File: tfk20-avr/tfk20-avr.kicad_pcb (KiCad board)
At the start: 4 copper layers, 76.2 x 115.9 mm, 122 parts, among them J1 USB_C_Receptacle_USB2.0, J2 AVR-ISP-6, SW1 Reset, U1 ATmega32U4-AU, U2 IS31FL3733-TQ, Y1 16MHz

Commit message: Finish routing
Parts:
- moved R13 8.08 mm to (181.9, 89.3), turned to 90 degrees
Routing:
- net GND: track 103.1 -> 236.1 mm, vias 16 -> 37
- net (no net): track 0.00 -> 21.8 mm
- net /tfk20 RGB Matrix/SW4: track 135.7 -> 146.7 mm, vias 16 -> 17
- net Net-(R13-Pad2): track 2.82 -> 7.60 mm
- net Net-(C8-Pad1): track 1.27 -> 5.77 mm
- net /tfk20 RGB Matrix/CS8: track 111.4 -> 115.2 mm, vias 10 -> 11
- net +5V: track 334.2 -> 336.9 mm
- net Net-(R7-Pad2): track 9.91 -> 12.3 mm
- net /COL_3: track 86.7 -> 88.1 mm
- net /tfk20 RGB Matrix/SW8: track 204.4 -> 203.2 mm
- net /tfk20 RGB Matrix/SW7: track 225.2 -> 224.4 mm
- net /RGB_MATRIX_SCL: track 31.7 -> 32.3 mm
- net /RGB_MATRIX_SDA: track 29.0 -> 29.6 mm
- net /XTAL2: vias 0 -> 2
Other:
- copper layers 4 -> 2

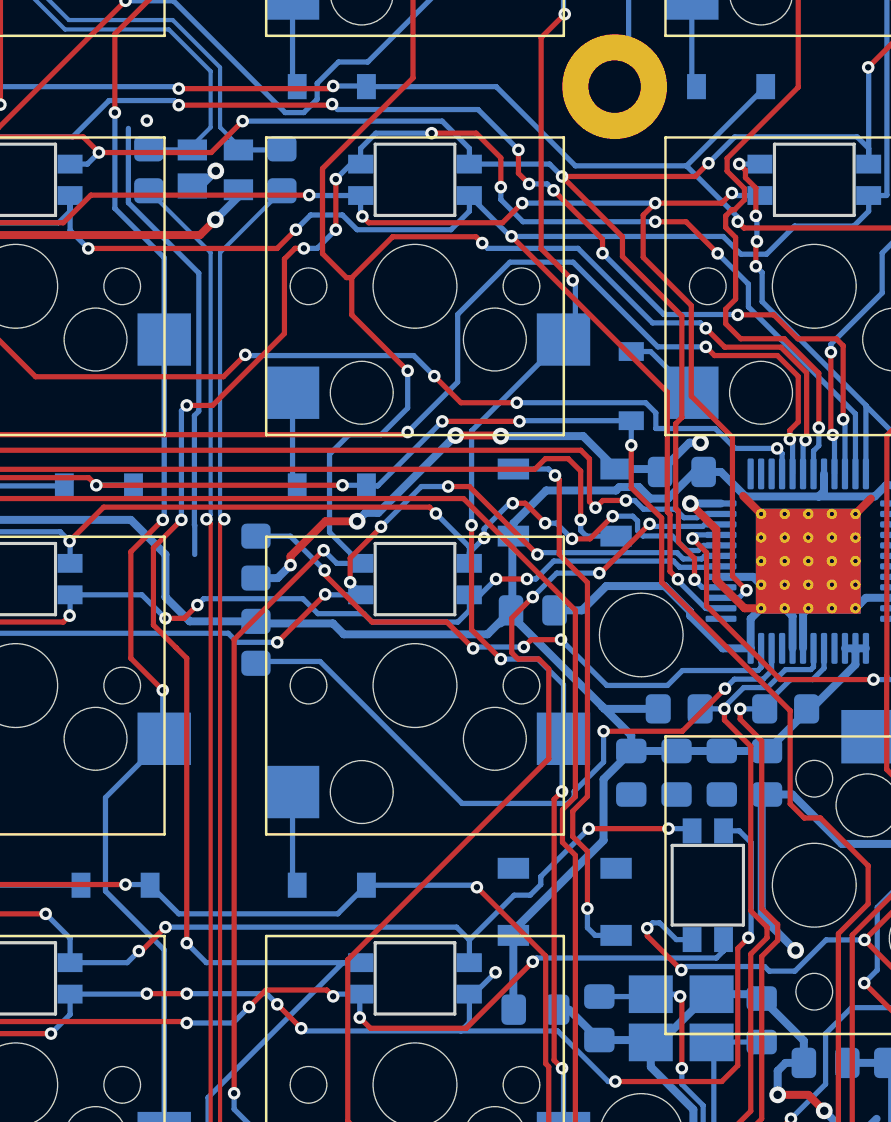
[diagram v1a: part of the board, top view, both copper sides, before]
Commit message: Add dimensions
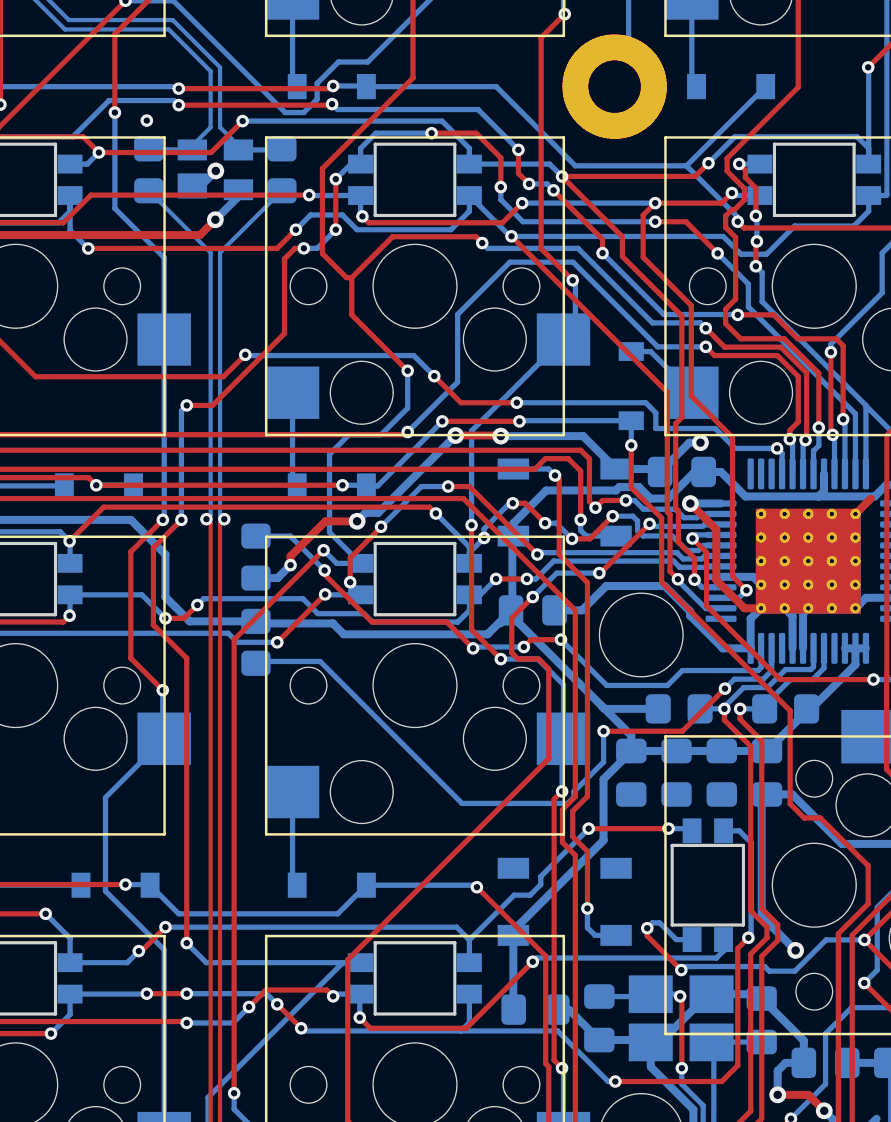
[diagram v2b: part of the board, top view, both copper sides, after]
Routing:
- net (no net): track 21.8 -> 0.00 mm
- net /tfk20 RGB Matrix/SW4: track 146.7 -> 145.2 mm, vias 17 -> 16
- net GND: track 236.1 -> 234.9 mm

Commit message: Tweak some things
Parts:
- moved SW1 1.19 mm to (126.2, 78.2)
- moved J1 0.56 mm to (125.8, 40.1)
- moved R1 0.13 mm to (125.3, 85.3)
- moved R2 0.13 mm to (120.7, 46.4)
- moved R3 0.13 mm to (131.7, 46.4)
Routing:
- net GND: track 234.9 -> 240.5 mm, vias 37 -> 38
- net /tfk20 RGB Matrix/SW9: track 246.7 -> 249.6 mm
- net /RESET: track 143.6 -> 144.3 mm
- net /tfk20 RGB Matrix/SW5: track 149.9 -> 150.5 mm
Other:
- board size 76.2 x 115.9 mm -> 76.2 x 115.5 mm
- board text added: "Inner hole diameter: 2.5mm"
- board text added: "tfk20 biosmanager Rev. 0"

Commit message: Add signature
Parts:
- added G1: LOGO, biosmanager:biosmanager_logo_filled_alt, F.Cu at (145.3, 77.0)
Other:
- board text added: "Rev. 0"
- board text added: "tfk20-avr Designed by biosmanager"
- board text removed: "tfk20 biosmanager Rev. 0"

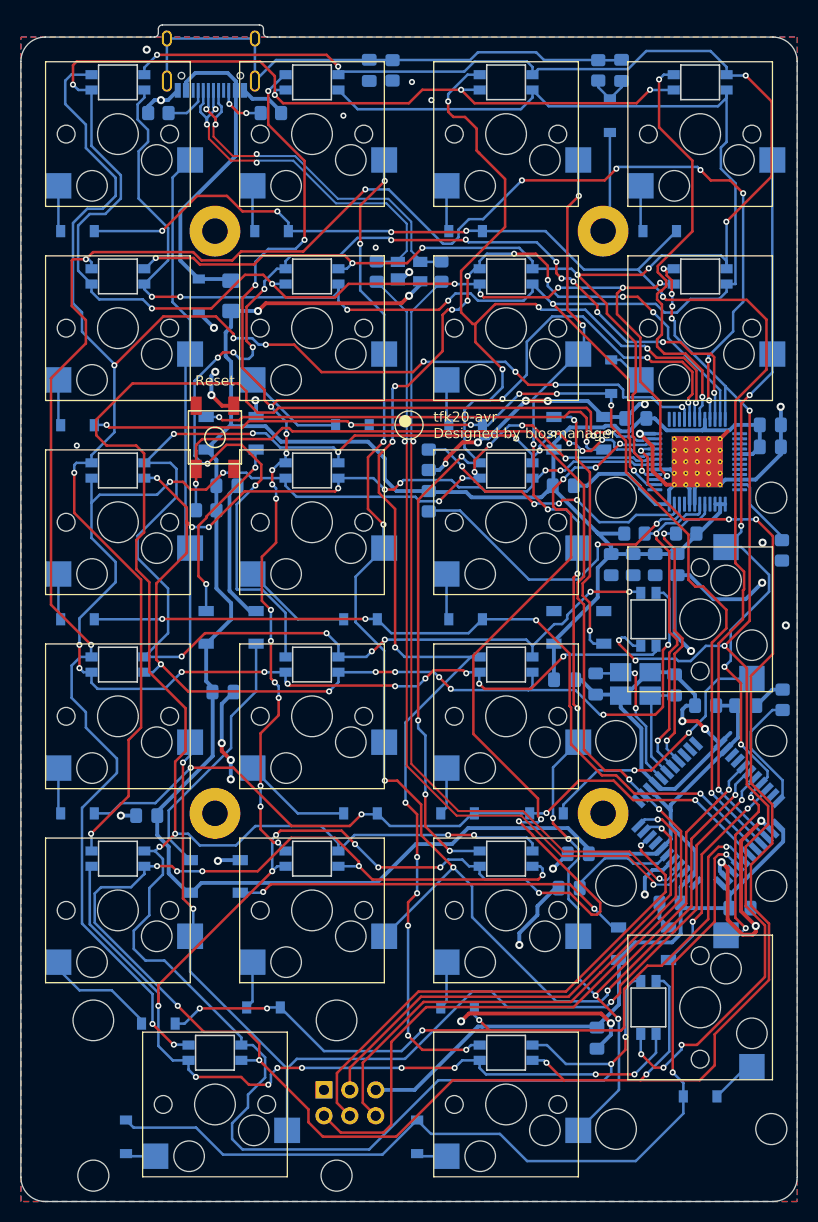
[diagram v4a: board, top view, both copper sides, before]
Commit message: Start new 4 layer layout
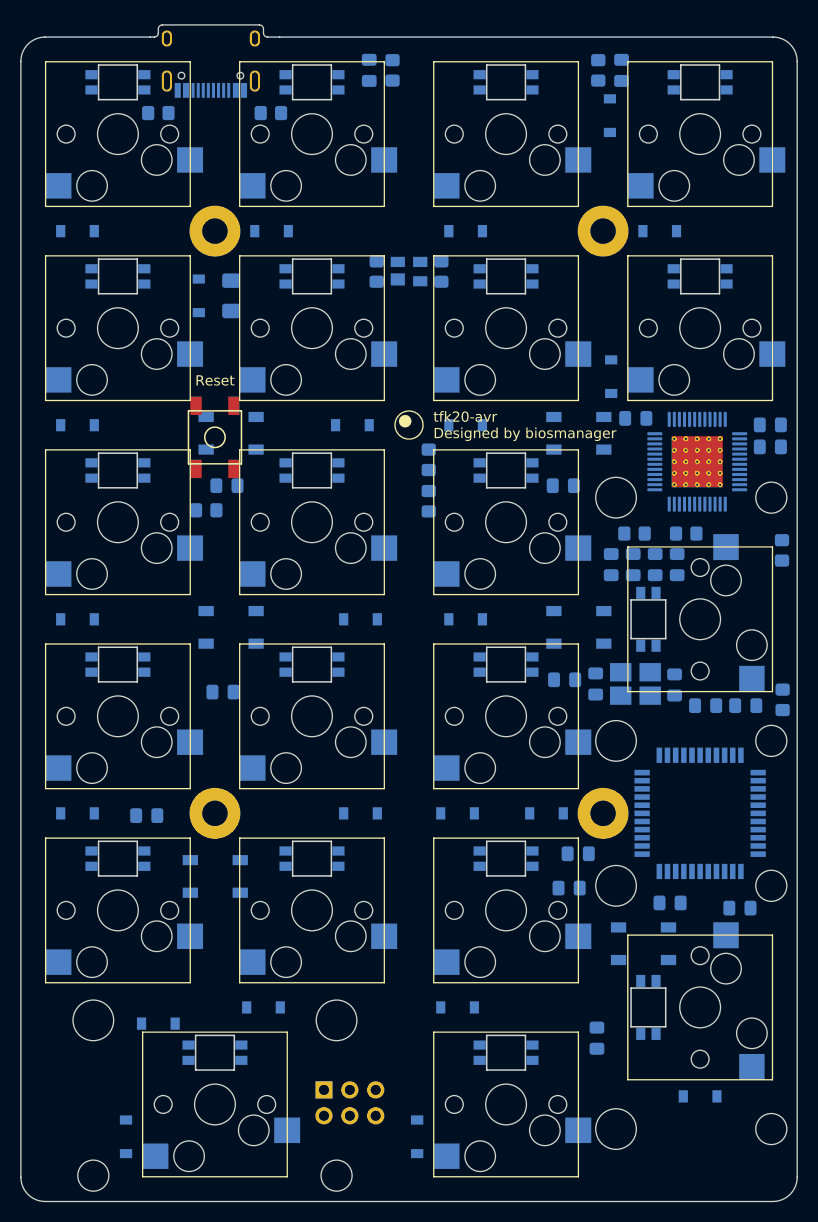
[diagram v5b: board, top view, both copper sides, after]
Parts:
- moved U1 0.79 mm to (173.8, 115.1), turned to 0 degrees
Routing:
- net +5V: track 336.9 -> 0.00 mm, vias 2 -> 0
- net /tfk20 RGB Matrix/SW9: track 249.6 -> 0.00 mm, vias 8 -> 0
- net GND: track 240.5 -> 0.00 mm, vias 38 -> 0
- net /tfk20 RGB Matrix/SW7: track 224.4 -> 0.00 mm, vias 12 -> 0
- net /tfk20 RGB Matrix/SW8: track 203.2 -> 0.00 mm, vias 20 -> 0
- net /tfk20 RGB Matrix/CS5: track 192.1 -> 0.00 mm, vias 11 -> 0
- net /tfk20 RGB Matrix/SW2: track 180.8 -> 0.00 mm, vias 12 -> 0
- net /tfk20 RGB Matrix/SW3: track 174.9 -> 0.00 mm, vias 10 -> 0
- net /tfk20 RGB Matrix/SW1: track 173.0 -> 0.00 mm, vias 6 -> 0
- net /COL_0: track 165.4 -> 0.00 mm, vias 4 -> 0
- net /tfk20 RGB Matrix/CS1: track 156.3 -> 0.00 mm, vias 9 -> 0
- net /tfk20 RGB Matrix/SW5: track 150.5 -> 0.00 mm, vias 18 -> 0
- net /tfk20 RGB Matrix/SW4: track 145.2 -> 0.00 mm, vias 16 -> 0
- net /RESET: track 144.3 -> 0.00 mm, vias 3 -> 0
- net /tfk20 RGB Matrix/CS2: track 142.7 -> 0.00 mm, vias 19 -> 0
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- added copper zone on POWER, net +5V
- added copper zone on GND, net GND
- removed copper zone on B.Cu, net GND
- removed copper zone on F.Cu, net GND
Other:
- copper layers 2 -> 4
- net class Default: clearance 0.15 -> 0.1524; trace_width 0.25 -> 0.254
- net class Power: clearance 0.15 -> 0.1524
- rule trace_clearance: 0.15 -> 0.1524

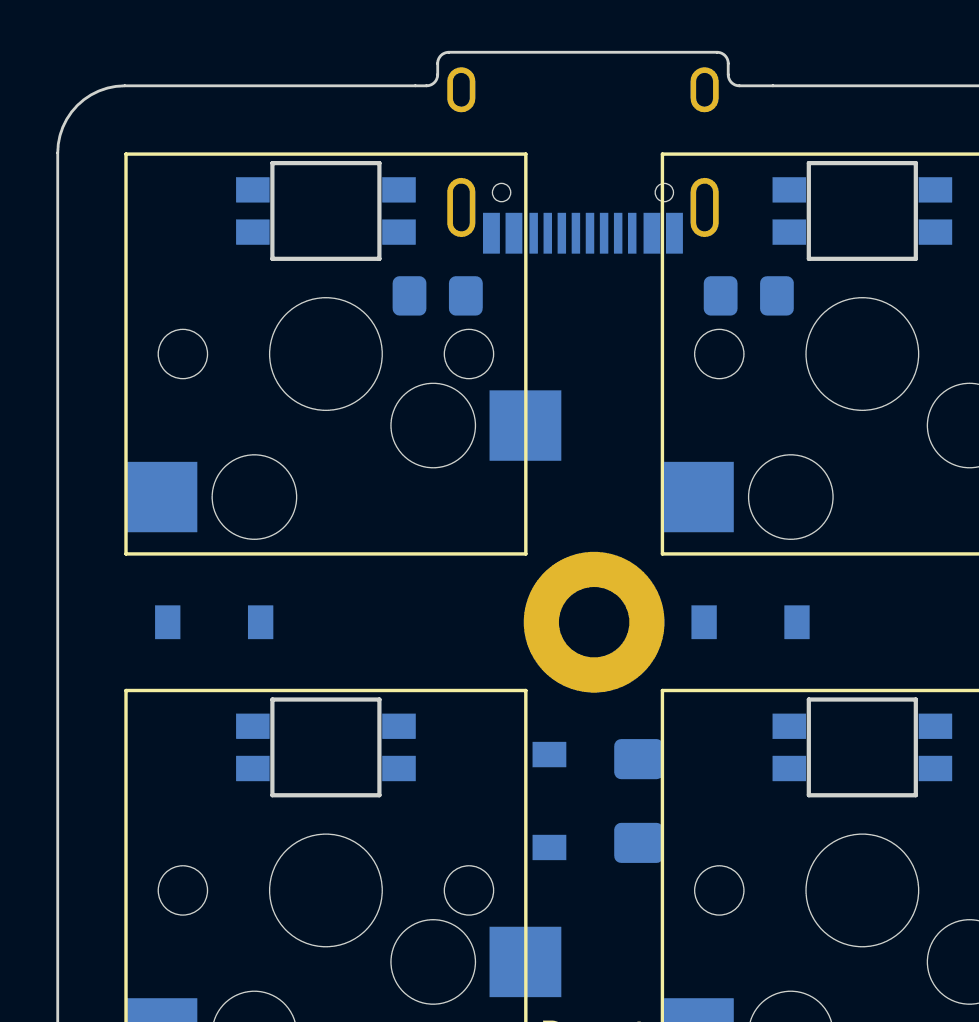
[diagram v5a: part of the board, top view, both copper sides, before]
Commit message: Route VBUS
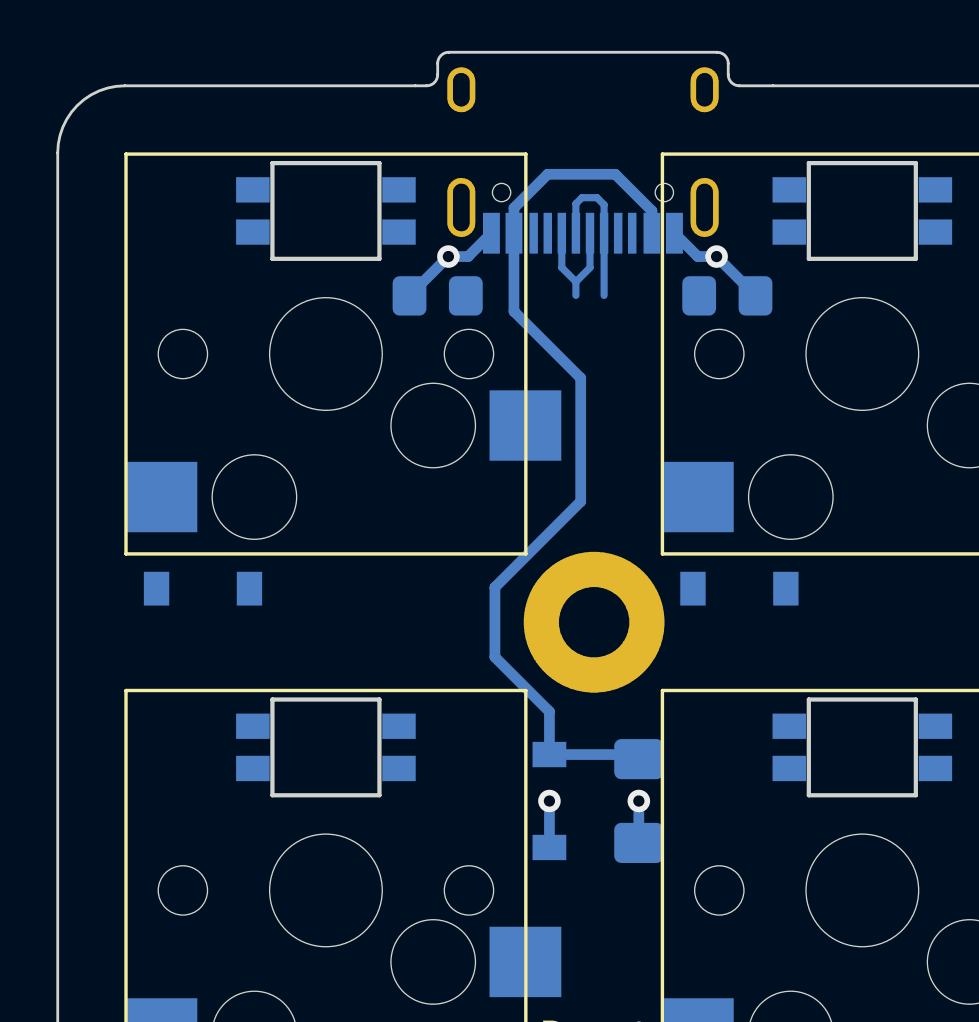
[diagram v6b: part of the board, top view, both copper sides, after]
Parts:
- moved D4 1.26 mm to (112.3, 56.8)
- moved D5 1.26 mm to (131.4, 56.8)
- moved R3 0.76 mm to (130.9, 46.4)
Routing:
- net VBUS: track 0.00 -> 32.4 mm
- net GND: track 0.00 -> 9.30 mm, vias 0 -> 3
- net /IN_USB_D+: track 0.00 -> 5.46 mm
- net /IN_USB_D-: track 0.00 -> 4.34 mm
- net +5V: track 0.00 -> 1.49 mm, vias 0 -> 1

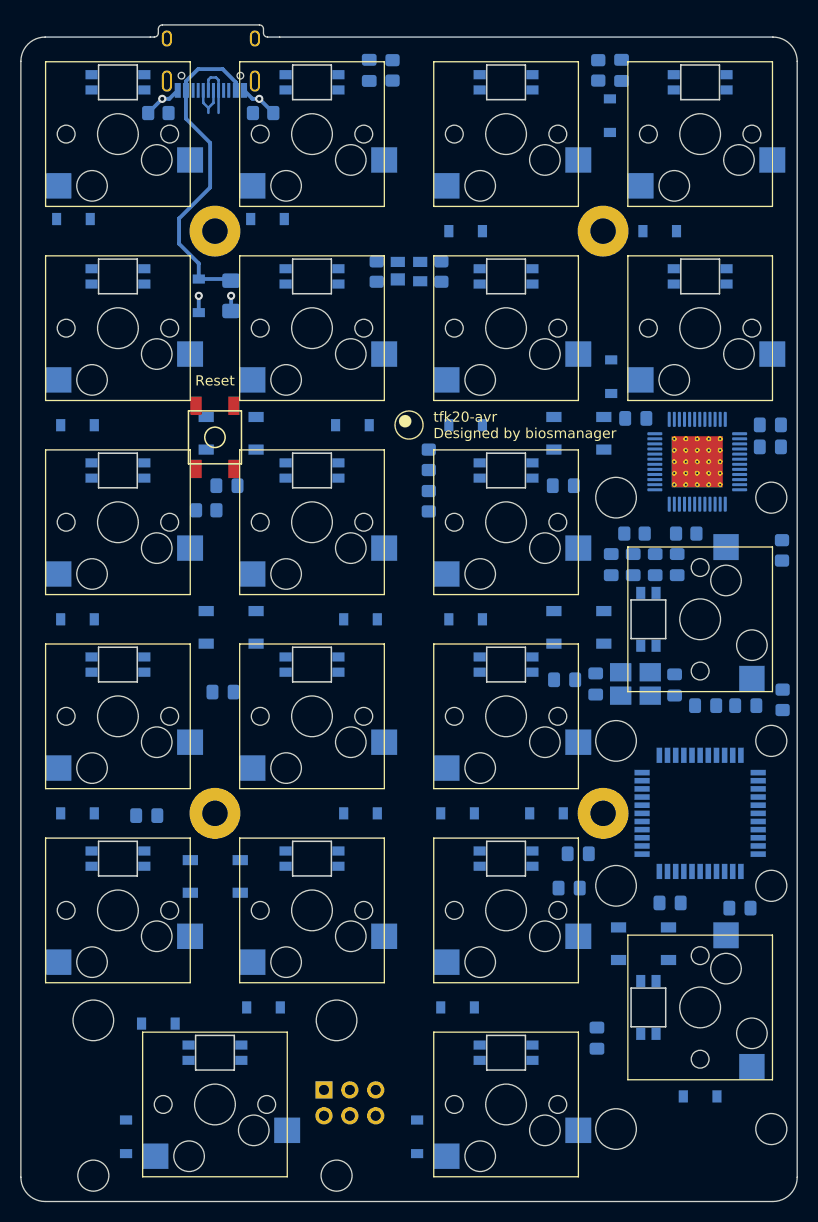
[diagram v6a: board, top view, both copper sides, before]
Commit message: Route PWR and GND
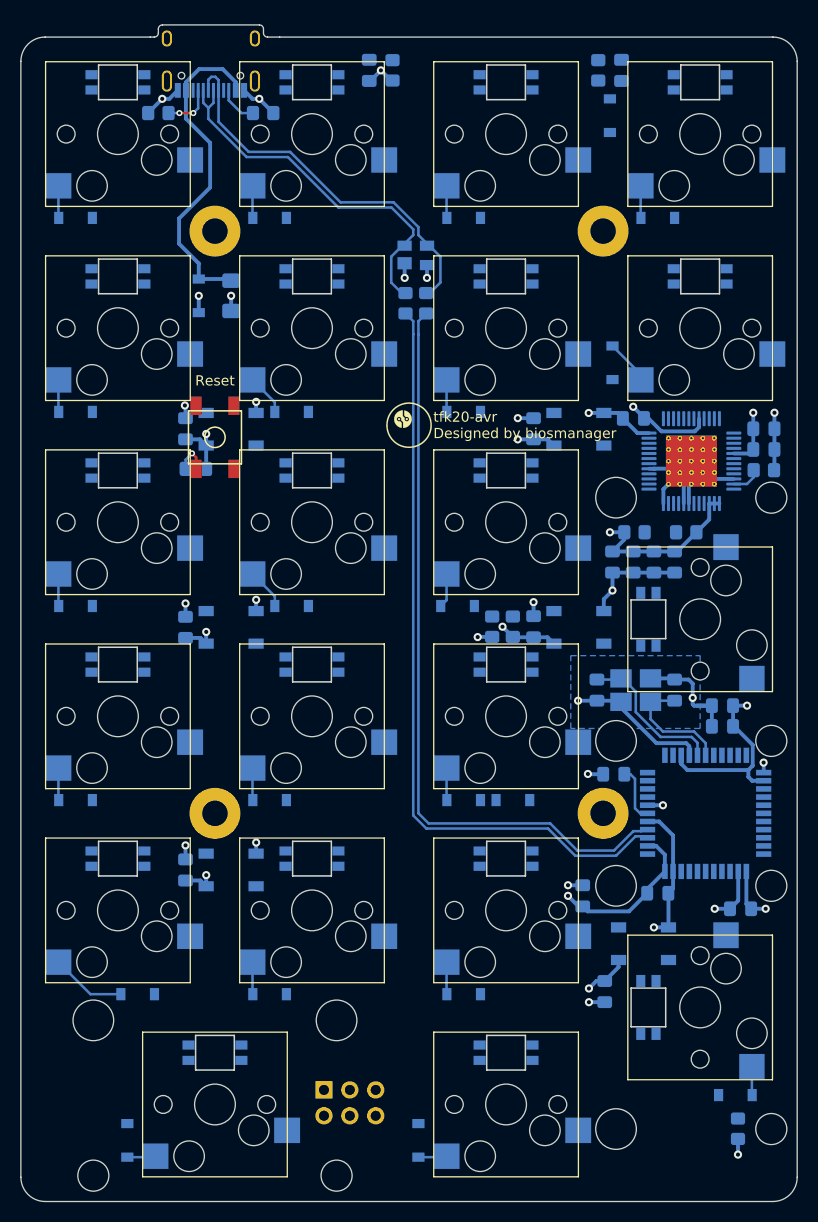
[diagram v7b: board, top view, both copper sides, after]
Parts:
- G1: footprint biosmanager:biosmanager_logo_filled_alt -> biosmanager:biosmanager_pcb
- H5, H6, H7: footprint Mounting_Keyboard_Stabilizer:Stabilizer_Cherry_MX_2u -> Mounting_Keyboard_Stabilizer:Stabilizer_Cherry_MX_2u_CrtYd
- moved R7 42.3 mm to (177.5, 146.1), turned to 90 degrees
- moved R12 17.5 mm to (153.4, 96.8)
- moved R9 14.8 mm to (155.4, 96.8), turned to 90 degrees
- moved C7 12.0 mm to (165.4, 111.3)
- moved D16 9.02 mm to (131.6, 113.8)
- moved R13 8.07 mm to (180.1, 81.4), turned to 180 degrees
- moved C13 7.34 mm to (123.3, 96.8), turned to 90 degrees
- moved C14 6.91 mm to (123.3, 77.3), turned to 90 degrees
- moved D13 6.89 mm to (133.7, 94.7)
- moved C12 6.55 mm to (123.3, 120.7), turned to 90 degrees
- moved C15 6.31 mm to (157.5, 77.3), turned to 90 degrees
- moved D9 6.11 mm to (133.7, 75.7)
- moved C16 6.03 mm to (157.5, 96.8), turned to 90 degrees
- moved C11 4.64 mm to (164.5, 132.6)
- moved R6 4.20 mm to (144.9, 65.0)
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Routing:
- net GND: track 9.30 -> 123.7 mm, vias 3 -> 26
- net +5V: track 1.49 -> 101.8 mm, vias 1 -> 15
- net /MCU_USB_D-: track 0.00 -> 75.1 mm
- net /MCU_USB_D+: track 0.00 -> 74.2 mm
- net /IN_USB_D-: track 4.34 -> 37.6 mm
- net /IN_USB_D+: track 5.46 -> 38.7 mm
- net /XTAL2: track 0.00 -> 14.9 mm
- net /XTAL1: track 0.00 -> 11.7 mm
- net Net-(D19-Pad2): track 0.00 -> 7.43 mm
- net Net-(C7-Pad1): track 0.00 -> 5.56 mm
- net Net-(J1-PadA5): track 0.00 -> 4.85 mm, vias 0 -> 2
- net Net-(D11-Pad2): track 0.00 -> 4.48 mm
- net Net-(D13-Pad2): track 0.00 -> 4.05 mm
- net Net-(D9-Pad2): track 0.00 -> 4.05 mm
- net Net-(J1-PadB5): track 0.00 -> 3.87 mm
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- added copper zone on B.Cu, net GND
